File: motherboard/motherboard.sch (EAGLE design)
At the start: 58 parts, among them IC1 USB6B1, Q1 MOSFET-NCHANNELPTH2, T1 2N3904, T2 2N3904, U1 LED_100V_BUCK, U2 LED_100V_BUCK, U3 LED_100V_BUCK, U4 LED_100V_BUCK, X1 USB_3P-85-32003-00X-1

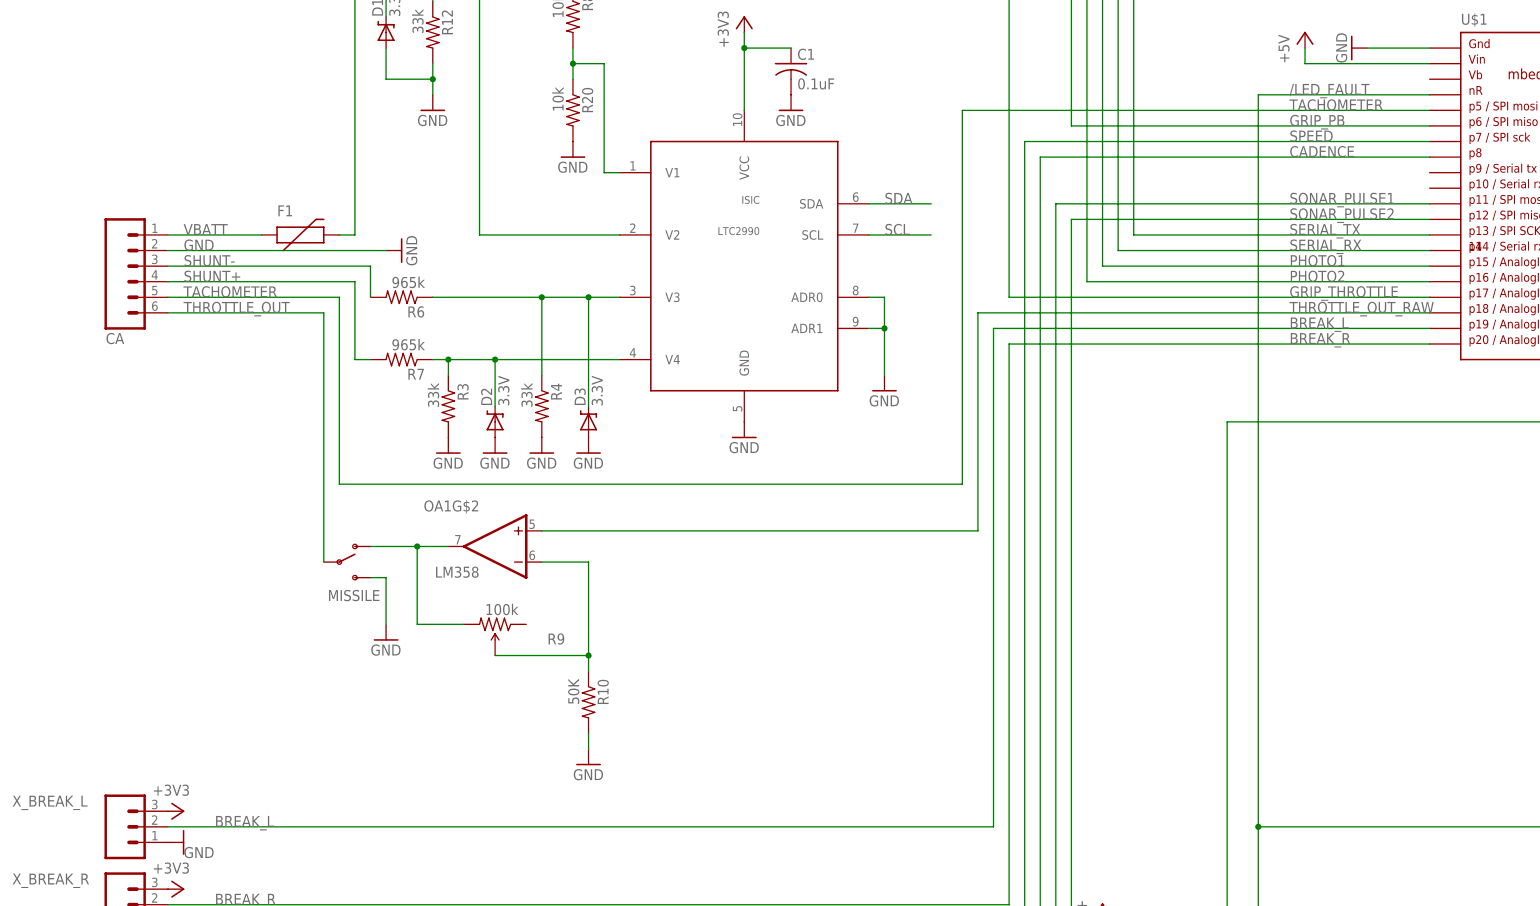
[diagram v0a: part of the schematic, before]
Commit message: Add driver for missile switch led and reexport files.
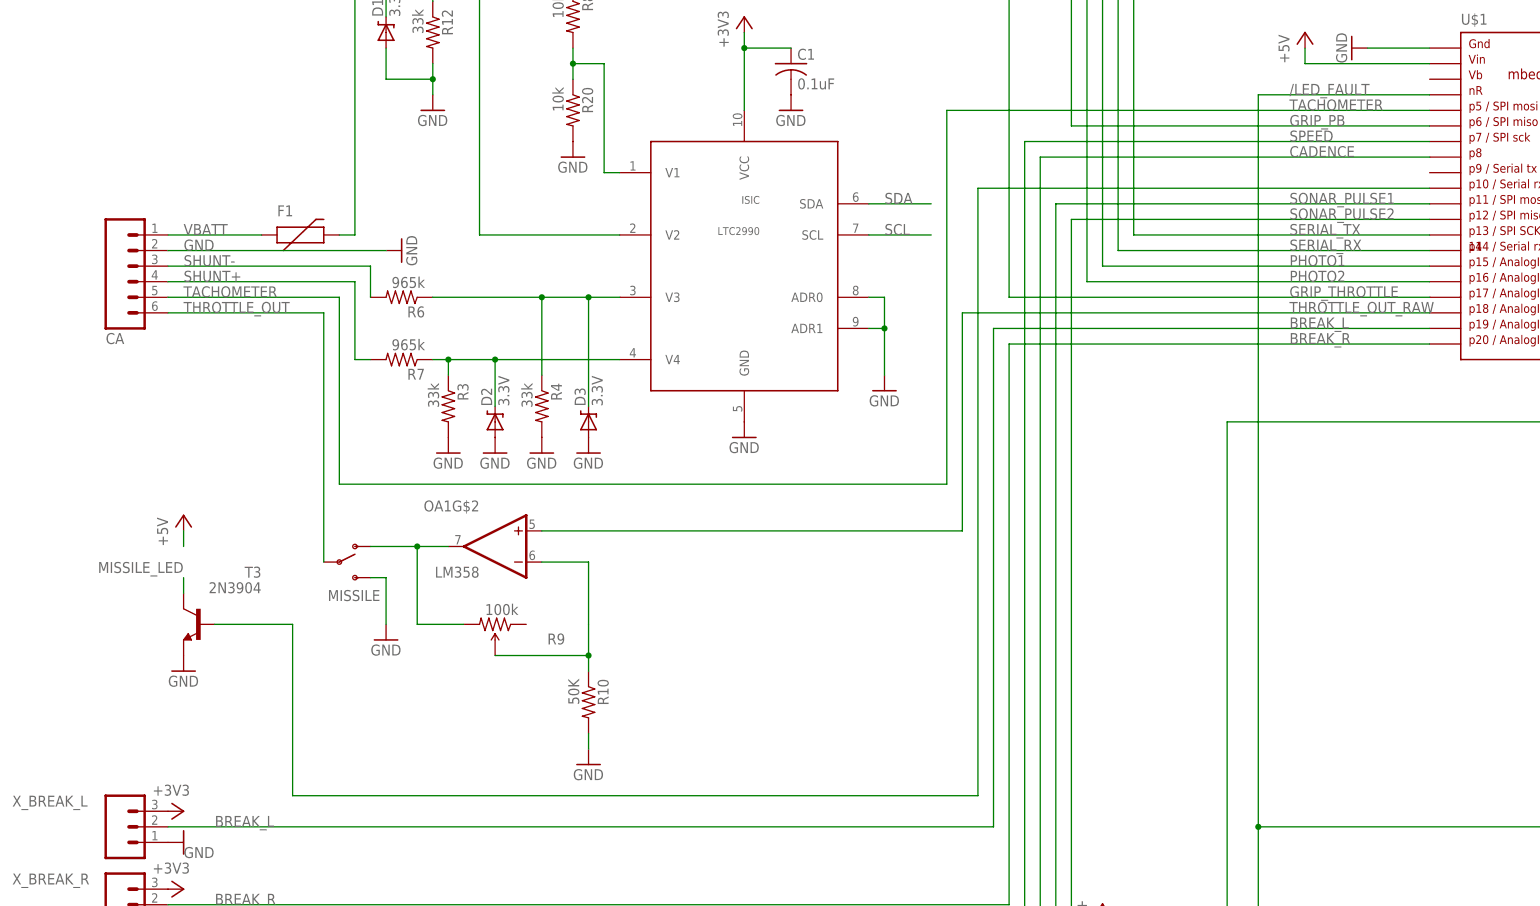
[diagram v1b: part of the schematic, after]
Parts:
- added T3: 2N3904, transistor:2N3904
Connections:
- new net MISSILE_LED: T3.C
- new net N$22: T3.B, U$1.P$10
- net GND: now also T3.E
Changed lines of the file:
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@@
 <part name="GND35" library="supply1" deviceset="GND" device=""/>
 <part name="P+8" library="supply1" deviceset="+5V" device=""/>
+<part name="T3" library="transistor" deviceset="2N3904" device=""/>
+<part name="GND36" library="supply1" deviceset="GND" device=""/>
+<part name="P+9" library="supply1" deviceset="+5V" device=""/>
 </parts>
 <sheets>
@@
 <instance part="GND35" gate="1" x="-177.8" y="274.32"/>
 <instance part="P+8" gate="1" x="-177.8" y="304.8"/>
+<instance part="T3" gate="G1" x="-238.76" y="198.12" rot="MR0"/>
+<instance part="GND36" gate="1" x="-241.3" y="190.5"/>
+<instance part="P+9" gate="1" x="-241.3" y="215.9"/>
 </instances>
 <busses>
@@
 <pinref part="R20" gate="G$1" pin="2"/>
 <pinref part="GND35" gate="1" pin="GND"/>
+</segment>
+<segment>
+<pinref part="T3" gate="G1" pin="E"/>
+<pinref part="GND36" gate="1" pin="GND"/>
 </segment>
 </net>
@@
 <pinref part="R8" gate="G$1" pin="1"/>
 <pinref part="P+8" gate="1" pin="+5V"/>
+</segment>
+<segment>
+<pinref part="P+9" gate="1" pin="+5V"/>
+<wire x1="-241.3" y1="213.36" x2="-241.3" y2="210.82" width="0.1524" layer="91"/>
 </segment>
 </net>
@@
 <label x="-241.3" y="251.46" size="1.778" layer="95"/>
 <wire x1="-215.9" y1="251.46" x2="-215.9" y2="220.98" width="0.1524" layer="91"/>
-<wire x1="-215.9" y1="220.98" x2="-114.3" y2="220.98" width="0.1524" layer="91"/>
-<wire x1="-114.3" y1="220.98" x2="-114.3" y2="281.94" width="0.1524" layer="91"/>
-<wire x1="-38.1" y1="281.94" x2="-114.3" y2="281.94" width="0.1524" layer="91"/>
+<wire x1="-215.9" y1="220.98" x2="-116.84" y2="220.98" width="0.1524" layer="91"/>
+<wire x1="-116.84" y1="220.98" x2="-116.84" y2="281.94" width="0.1524" layer="91"/>
+<wire x1="-38.1" y1="281.94" x2="-116.84" y2="281.94" width="0.1524" layer="91"/>
 </segment>
 </net>
@@
 <segment>
 <pinref part="U$1" gate="G$1" pin="P$18"/>
-<wire x1="-38.1" y1="248.92" x2="-111.76" y2="248.92" width="0.1524" layer="91"/>
-<wire x1="-111.76" y1="248.92" x2="-111.76" y2="213.36" width="0.1524" layer="91"/>
+<wire x1="-38.1" y1="248.92" x2="-114.3" y2="248.92" width="0.1524" layer="91"/>
+<wire x1="-114.3" y1="248.92" x2="-114.3" y2="213.36" width="0.1524" layer="91"/>
 <pinref part="OA1" gate="G$2" pin="+IN"/>
-<wire x1="-111.76" y1="213.36" x2="-182.88" y2="213.36" width="0.1524" layer="91"/>
+<wire x1="-114.3" y1="213.36" x2="-182.88" y2="213.36" width="0.1524" layer="91"/>
 <label x="-60.96" y="248.92" size="1.778" layer="95"/>
 </segment>
@@
 </segment>
 </net>
+<net name="MISSILE_LED" class="0">
+<segment>
+<pinref part="T3" gate="G1" pin="C"/>
+<wire x1="-241.3" y1="203.2" x2="-241.3" y2="205.74" width="0.1524" layer="91"/>
+<label x="-241.3" y="208.28" size="1.778" layer="95" rot="R180"/>
+</segment>
+</net>
+<net name="N$22" class="0">
+<segment>
+<pinref part="U$1" gate="G$1" pin="P$10"/>
+<wire x1="-38.1" y1="269.24" x2="-111.76" y2="269.24" width="0.1524" layer="91"/>
+<wire x1="-111.76" y1="269.24" x2="-111.76" y2="170.18" width="0.1524" layer="91"/>
+<wire x1="-111.76" y1="170.18" x2="-223.52" y2="170.18" width="0.1524" layer="91"/>
+<pinref part="T3" gate="G1" pin="B"/>
+<wire x1="-223.52" y1="170.18" x2="-223.52" y2="198.12" width="0.1524" layer="91"/>
+<wire x1="-223.52" y1="198.12" x2="-236.22" y2="198.12" width="0.1524" layer="91"/>
+</segment>
+</net>

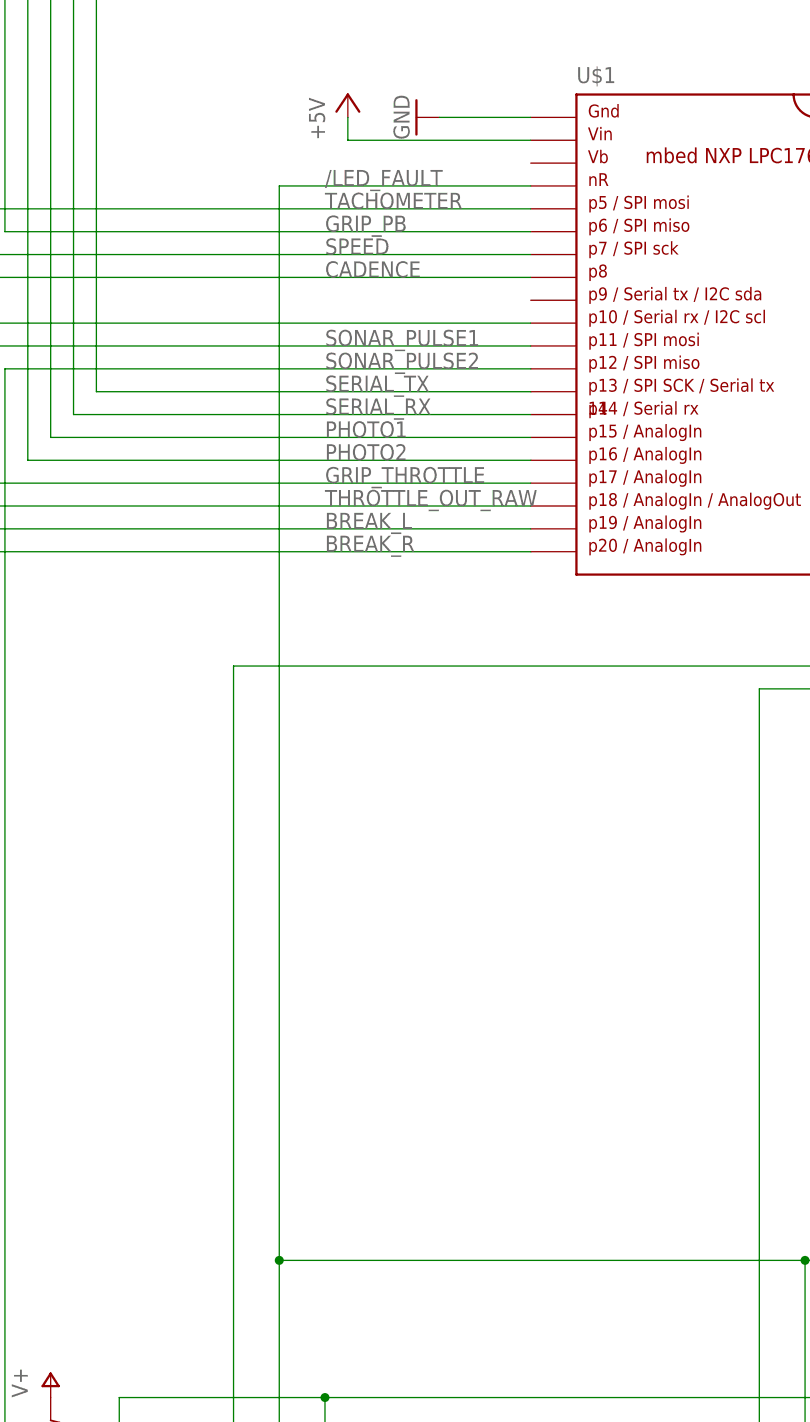
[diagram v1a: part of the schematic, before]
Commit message: Fix wiring of LED fault signal and leble LED indicator signal.
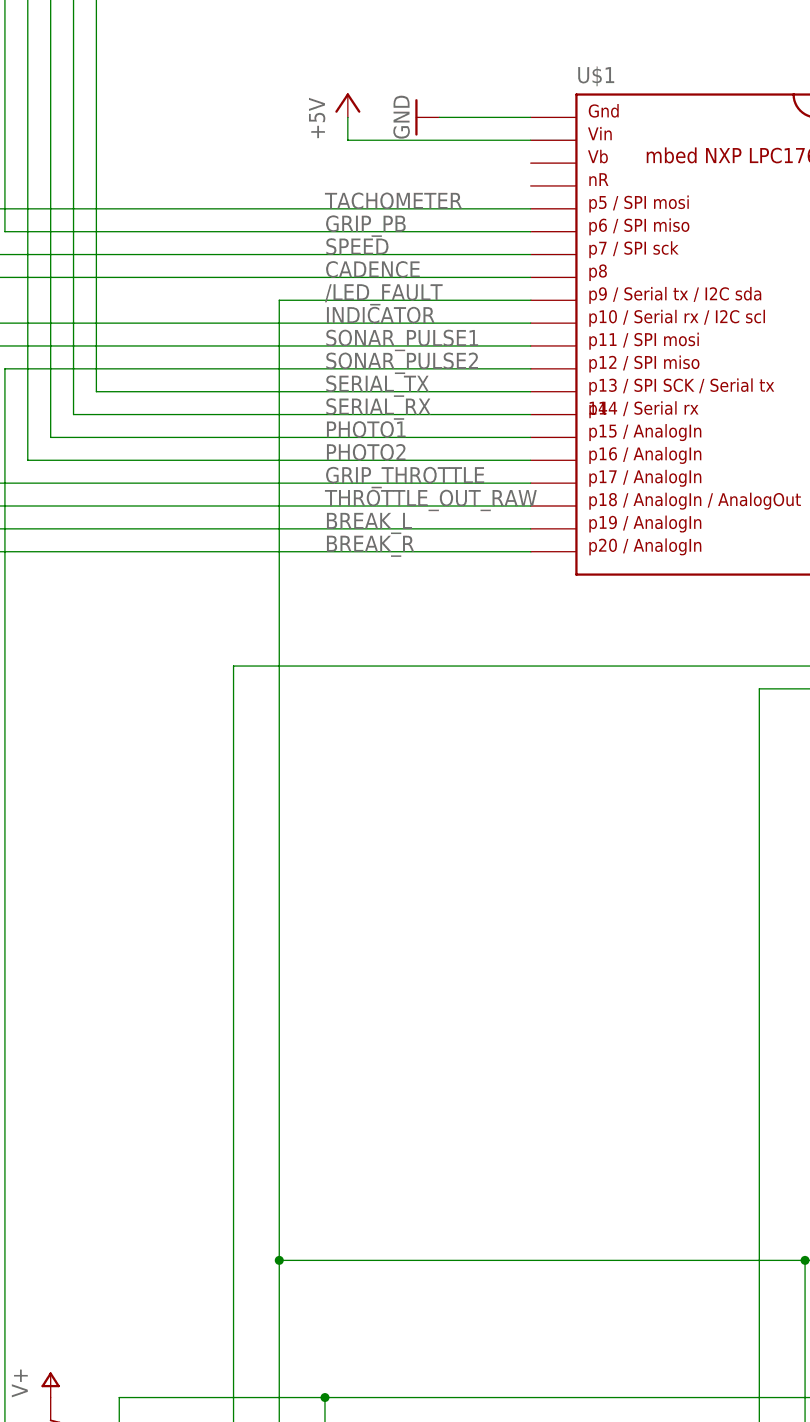
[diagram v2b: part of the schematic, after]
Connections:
- net N$22 renamed INDICATOR
- net /LED_FAULT: now also U$1.P$9
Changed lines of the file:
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@@
 <net name="/LED_FAULT" class="0">
 <segment>
-<wire x1="-66.04" y1="284.48" x2="-38.1" y2="284.48" width="0.1524" layer="91"/>
-<label x="-60.96" y="284.48" size="1.778" layer="95"/>
-<wire x1="-66.04" y1="284.48" x2="-66.04" y2="165.1" width="0.1524" layer="91"/>
+<label x="-60.96" y="271.78" size="1.778" layer="95"/>
 <pinref part="U3" gate="G$1" pin="/OPEN_LED"/>
+<wire x1="-66.04" y1="271.78" x2="-66.04" y2="165.1" width="0.1524" layer="91"/>
 <wire x1="101.6" y1="127" x2="91.44" y2="127" width="0.1524" layer="91"/>
 <wire x1="91.44" y1="127" x2="91.44" y2="165.1" width="0.1524" layer="91"/>
@@
 <label x="165.1" y="165.1" size="1.778" layer="95"/>
 <junction x="-66.04" y="165.1"/>
+<pinref part="U$1" gate="G$1" pin="P$9"/>
+<wire x1="-38.1" y1="271.78" x2="-66.04" y2="271.78" width="0.1524" layer="91"/>
 </segment>
 </net>
@@
 </segment>
 </net>
-<net name="N$22" class="0">
+<net name="INDICATOR" class="0">
 <segment>
 <pinref part="U$1" gate="G$1" pin="P$10"/>
@@
 <wire x1="-223.52" y1="170.18" x2="-223.52" y2="198.12" width="0.1524" layer="91"/>
 <wire x1="-223.52" y1="198.12" x2="-236.22" y2="198.12" width="0.1524" layer="91"/>
-</segment>
-</net>
+<label x="-60.96" y="269.24" size="1.778" layer="95"/>
+</segment>
+</net>
